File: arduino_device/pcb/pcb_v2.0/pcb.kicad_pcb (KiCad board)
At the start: 2 copper layers, 110.5 x 51.5 mm, 13 parts, among them SW1 SW_Push

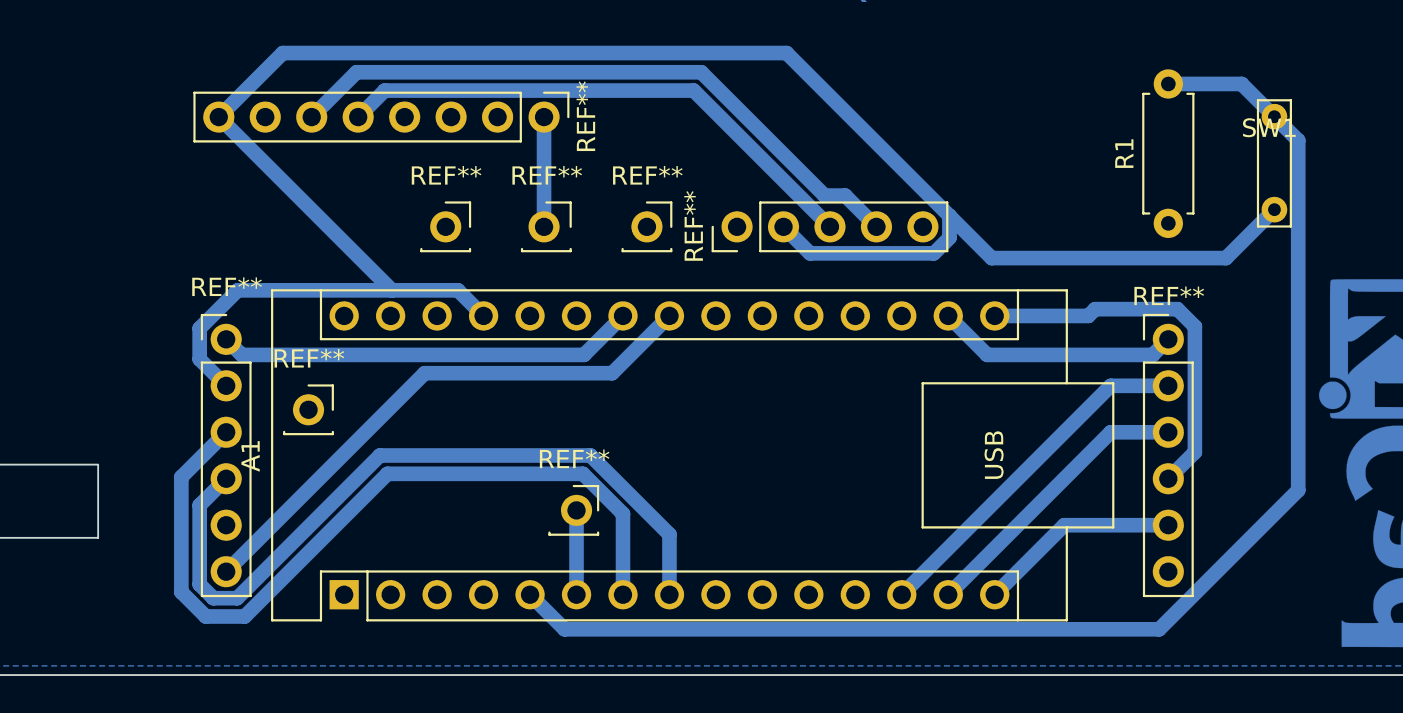
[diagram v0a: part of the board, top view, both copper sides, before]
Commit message: Arduino device -Test programs (Button, RTC, IMU, GPS) -Update PCB
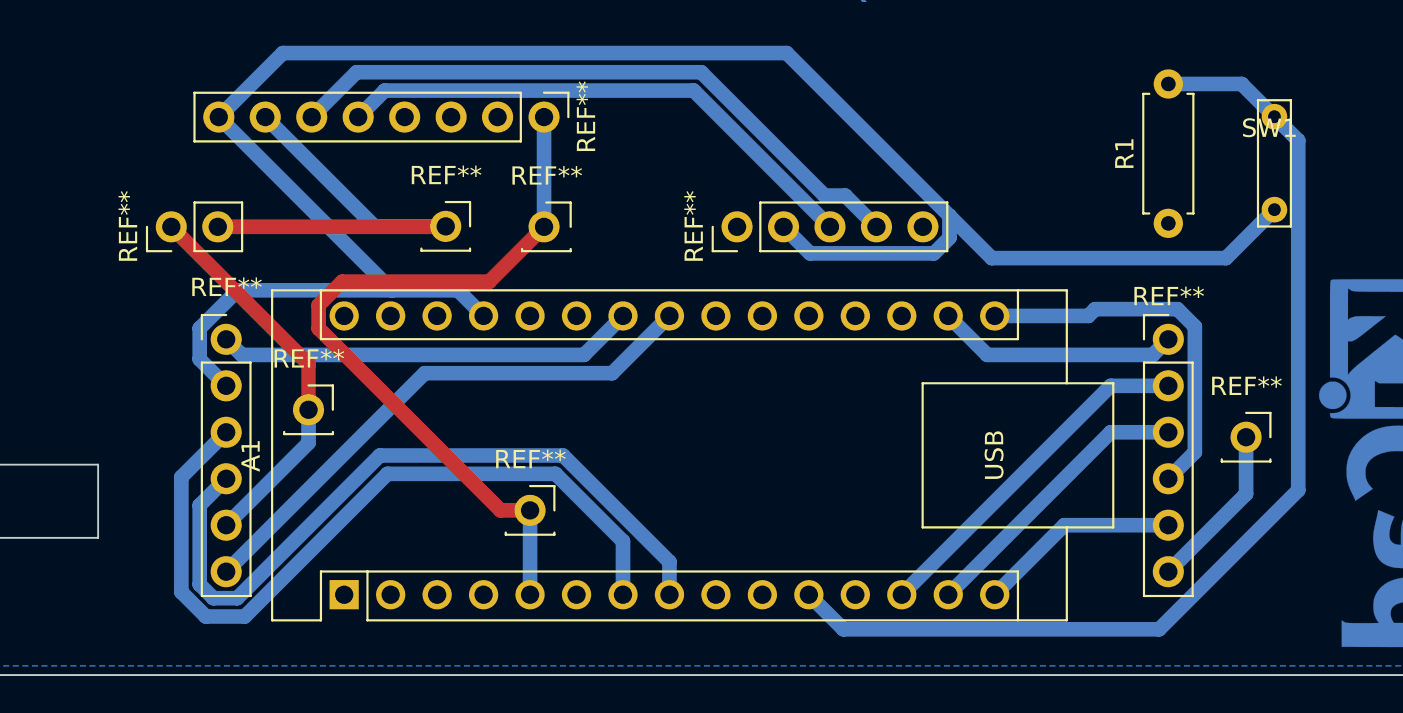
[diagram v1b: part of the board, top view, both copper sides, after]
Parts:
- added REF**: PinHeader_1x02_P2.54mm_Vertical, Connector_PinHeader_2.54mm:PinHeader_1x02_P2.54mm_Vertical, F.Cu at (107.0, 91.5)
- moved REF** 45.2 mm to (165.8, 103.0)
- moved REF** 11.0 mm to (122.0, 91.5)
- moved REF** 2.39 mm to (126.6, 107.0)
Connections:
- A1 pad 11: unconnected-(A1-Pad11) -> BUTTON
- A1 pad 5: BUTTON -> INTERRUPT
- A1 pad 6: INTERRUPT -> unconnected-(A1-Pad6)
- SW1 pad 1: 5v -> BUTTON
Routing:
- net Earth: track 0.00 -> 55.2 mm
- net INTERRUPT: track 10.6 -> 41.7 mm
- net BUTTON: track 73.4 -> 58.2 mm
- net GPS_RECEIVE: track 43.0 -> 42.1 mm
- net GPS_TRANSMIT: track 40.7 -> 39.8 mm

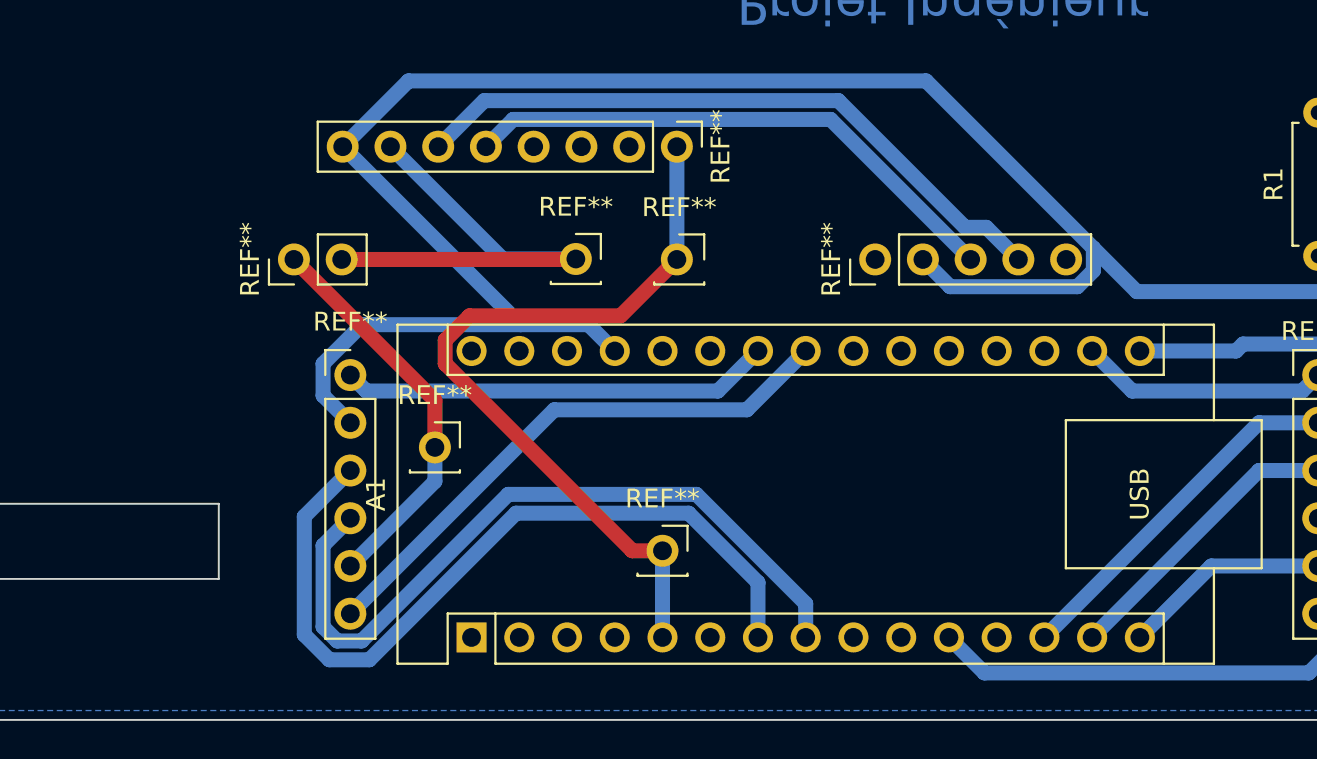
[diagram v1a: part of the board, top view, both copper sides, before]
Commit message: PCB update: -SDA and SDL lines -GPS testing
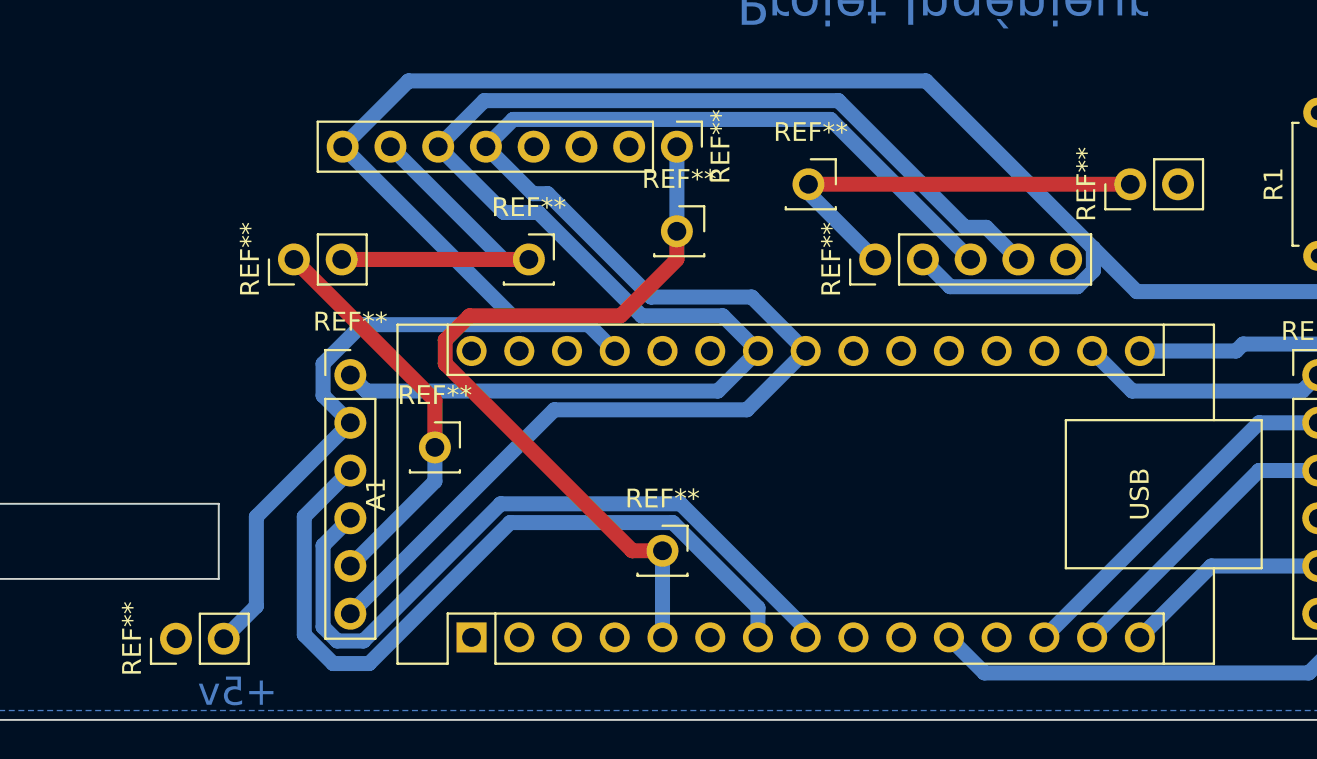
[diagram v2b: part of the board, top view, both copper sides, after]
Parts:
- added REF**: PinHeader_1x02_P2.54mm_Vertical, Connector_PinHeader_2.54mm:PinHeader_1x02_P2.54mm_Vertical, F.Cu at (100.7, 111.7)
- added REF**: PinSocket_1x01_P2.54mm_Vertical, Connector_PinSocket_2.54mm:PinSocket_1x01_P2.54mm_Vertical, F.Cu at (134.5, 87.5)
- added REF**: PinHeader_1x02_P2.54mm_Vertical, Connector_PinHeader_2.54mm:PinHeader_1x02_P2.54mm_Vertical, F.Cu at (151.5, 87.5)
- moved REF** 2.50 mm to (119.5, 91.5)
- moved REF** 1.50 mm to (127.5, 90.0)
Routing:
- net SDA: track 59.5 -> 81.0 mm
- net SCL: track 58.3 -> 79.8 mm
- net Earth: track 55.2 -> 72.8 mm
- net 5v: track 110.3 -> 124.6 mm
- net GPS_TRANSMIT: track 39.8 -> 38.6 mm
- net GPS_RECEIVE: track 42.1 -> 41.1 mm
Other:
- board text added: "+5v"

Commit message: First acceleration measures
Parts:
- removed the REF** at (173.7, 104.5)
- added REF**: KiCad-Logo2_5mm_Copper, Symbol:KiCad-Logo2_5mm_Copper, B.Cu at (89.0, 68.5)
- added REF**: Symbol_HighVoltage_Type2_CopperTop_VerySmall, Symbol:Symbol_HighVoltage_Type2_CopperTop_VerySmall, B.Cu at (175.4, 105.0)
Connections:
- SW1 pad 1: BUTTON -> 5v
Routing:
- net Earth: vias 0 -> 3
- net (no net): vias 0 -> 1
